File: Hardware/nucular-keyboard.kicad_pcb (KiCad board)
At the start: 2 copper layers, 48 x 25 mm, 34 parts, among them IC1 STM32L052R6Tx, J1 JAE_AA01B-S040VA1, J2 JAE_KX14-40K2D, J3 CONN_01X16, J4 CONN_01X03, Q1 IRLML6402, U1 MCP1700T-3302E/MB

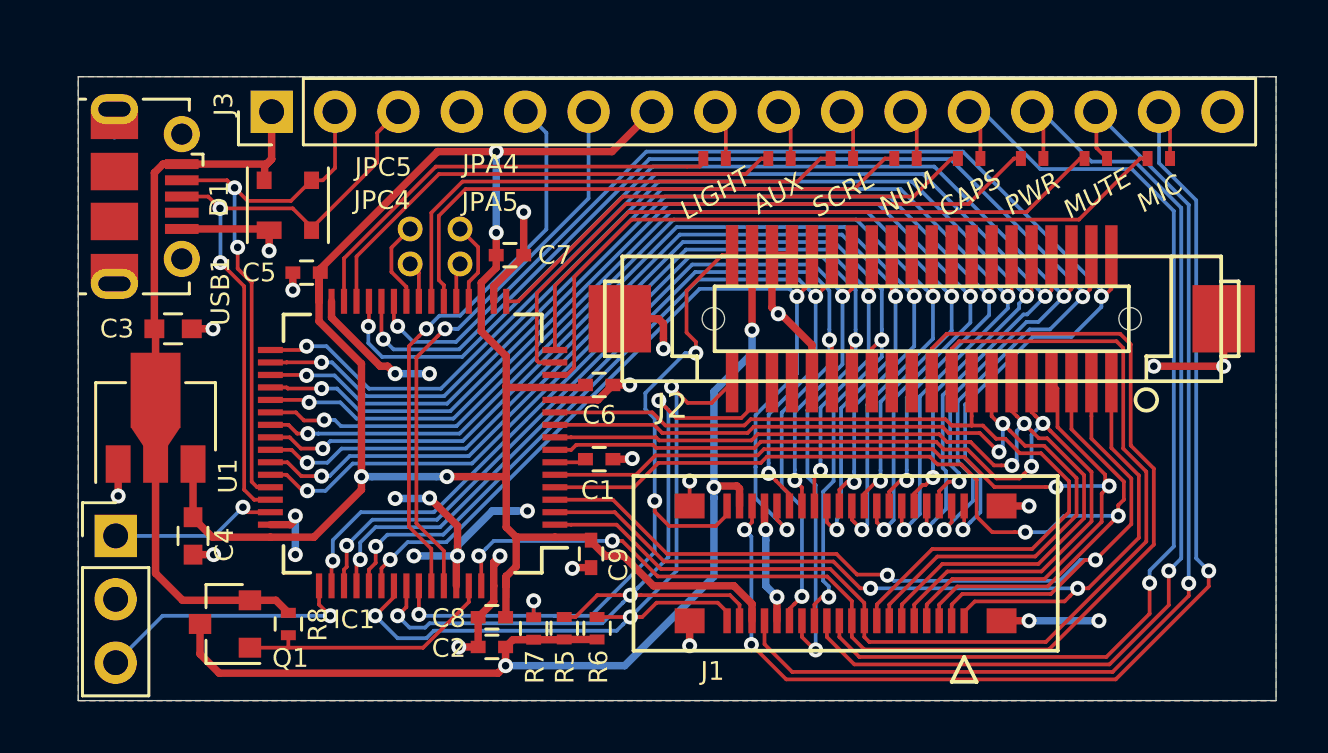
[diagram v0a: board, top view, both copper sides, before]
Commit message: Updated all footprints
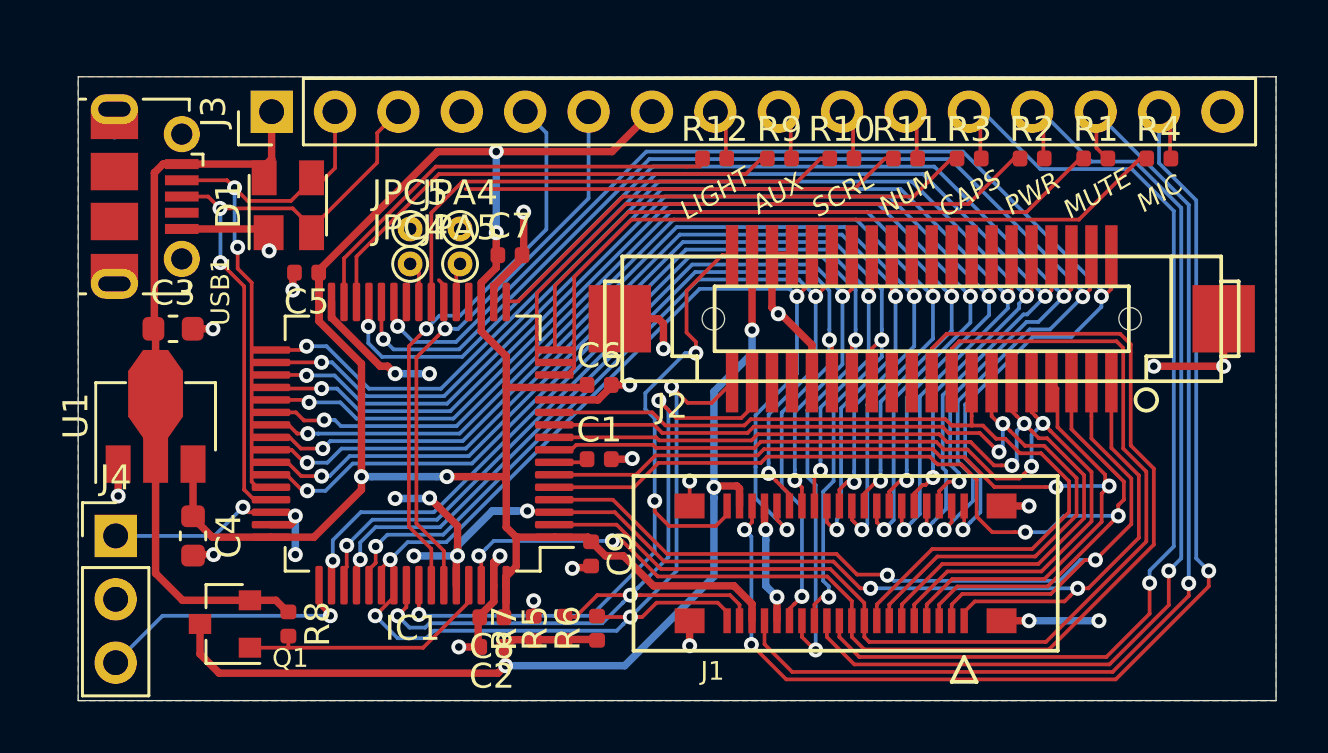
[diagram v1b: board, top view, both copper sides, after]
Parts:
- C1, C2, C5, C6, C7, C8, C9: footprint Capacitors_SMD:C_0402 -> Capacitor_SMD:C_0402_1005Metric
- C3, C4: footprint Capacitors_SMD:C_0603 -> Capacitor_SMD:C_0603_1608Metric
- D1: footprint 000-Modules:SOT143B -> Package_TO_SOT_SMD:SOT-143
- IC1: footprint Housings_QFP:LQFP-64_10x10mm_Pitch0.5mm -> Package_QFP:LQFP-64_10x10mm_P0.5mm
- J3: footprint Pin_Headers:Pin_Header_Straight_1x16_Pitch2.54mm -> Connector_PinHeader_2.54mm:PinHeader_1x16_P2.54mm_Vertical
- J4: footprint Pin_Headers:Pin_Header_Straight_1x03_Pitch2.54mm -> Connector_PinHeader_2.54mm:PinHeader_1x03_P2.54mm_Vertical
- JPA4, JPA5, JPC4, JPC5: footprint Wire_Pads:SolderWirePad_single_0-8mmDrill -> TestPoint:TestPoint_THTPad_D1.0mm_Drill0.5mm
- Q1: footprint TO_SOT_Packages_SMD:SOT-23 -> Package_TO_SOT_SMD:SOT-23
- R1, R10, R11, R12, R2, R3, R4, R9: footprint Resistors_SMD:R_0402_NoSilk -> Resistor_SMD:R_0402_1005Metric
- R5, R6, R7, R8: footprint Resistors_SMD:R_0402 -> Resistor_SMD:R_0402_1005Metric
- U1: footprint 000-Modules:SOT89-3 -> Package_TO_SOT_SMD:SOT-89-3
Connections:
- J2 pad 21: Net-(J2-Pad21) -> (no net)
- J2 pad 23: Net-(J2-Pad23) -> (no net)
- J2 pad 33: Net-(J2-Pad33) -> (no net)
- J2 pad 35: Net-(J2-Pad35) -> (no net)
- USB1 pad 4: Net-(USB1-Pad4) -> (no net)
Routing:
- net /LED_NUM: track 22.7 -> 18.6 mm
- net Net-(IC1-Pad25): track 3.46 -> 0.00 mm
- net Net-(IC1-Pad20): track 3.36 -> 0.00 mm

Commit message: Fixed some clearances
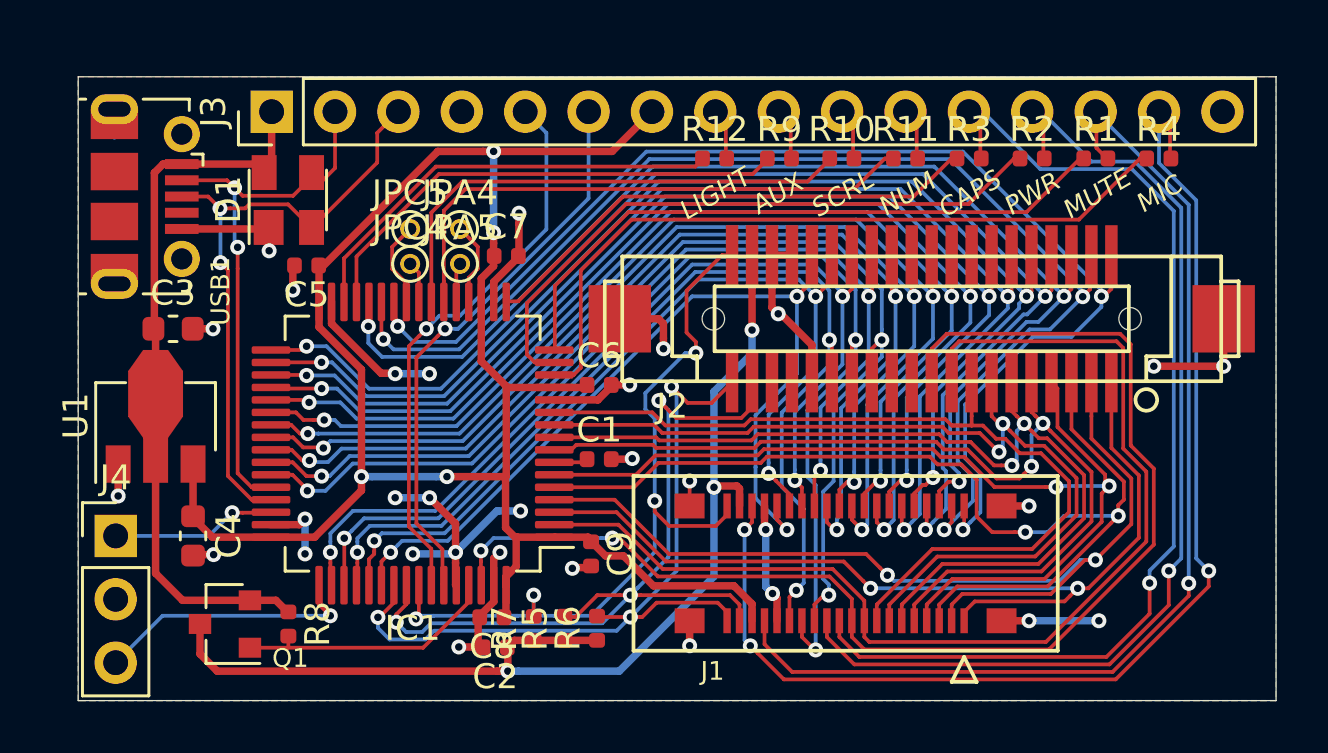
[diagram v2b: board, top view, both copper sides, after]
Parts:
- moved C5 0.29 mm to (69.2, 67.6)
- moved D1 0.21 mm to (68.4, 64.9)
- moved C7 0.15 mm to (77.2, 67.2)
- moved C2 0.13 mm to (76.7, 82.9)
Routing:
- net /LED_NUM: track 18.6 -> 22.6 mm
- net Net-(IC1-Pad25): track 0.00 -> 3.46 mm
- net Net-(IC1-Pad20): track 0.00 -> 3.37 mm
- net GND: track 69.6 -> 67.9 mm
- net VCC: track 77.1 -> 75.9 mm
- net /TP4_RESET: track 31.6 -> 32.4 mm

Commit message: Finished routing
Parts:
- C1, C2, C5, C6, C7, C8, C9: footprint Capacitor_SMD:C_0402_1005Metric -> Capacitor_SMD:C_0603_1608Metric
- R1, R10, R11, R12, R2, R3, R4, R5, R6, R7, R8, R9: footprint Resistor_SMD:R_0402_1005Metric -> Resistor_SMD:R_0603_1608Metric
- moved C2 5.97 mm to (70.7, 82.9), turned to 90 degrees
- moved R12 2.65 mm to (82.9, 63.0)
- moved R9 2.20 mm to (85.9, 63.0)
- moved R10 1.72 mm to (88.9, 63.0)
- moved R11 1.23 mm to (91.9, 63.0)
- moved C8 1.13 mm to (75.6, 82.2)
- moved C6 1.00 mm to (81.7, 73.0)
- moved R7 0.91 mm to (77.9, 82.9)
- moved R6 0.84 mm to (80.9, 82.9)
- moved R5 0.84 mm to (79.4, 82.9)
- moved R4 0.82 mm to (104.1, 63.0)
- moved C1 0.79 mm to (81.7, 75.3)
- moved R3 0.75 mm to (95.0, 63.0)
- moved J3 0.69 mm to (67.8, 60.7)
- moved D1 0.63 mm to (68.5, 64.3)
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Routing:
- net GND: track 67.9 -> 62.5 mm, vias 31 -> 26
- net /+5V_TP: track 43.6 -> 40.5 mm
- net /LED_LIGHT: track 17.8 -> 15.2 mm
- net /LED_AUX: track 19.9 -> 17.8 mm
- net VCC: track 75.9 -> 77.7 mm
- net /LED_LIGHT_R: track 2.02 -> 3.80 mm
- net /LED_MIC_R: track 48.3 -> 49.8 mm
- net /USB_DM: track 22.2 -> 23.7 mm
- net /LED_SCROLL: track 20.5 -> 19.0 mm
- net /LED_MUTE_R: track 42.7 -> 44.1 mm
- net /TP4_PWR: track 10.7 -> 11.9 mm
- net Net-(IC1-Pad20): track 3.37 -> 4.34 mm
- net /LED_NUM: track 22.6 -> 21.7 mm
- net /LED_MIC: track 29.7 -> 30.5 mm
- net /LED_AUX_R: track 2.07 -> 2.88 mm
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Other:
- board size 48 x 25 mm -> 48 x 26 mm

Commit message: Moved references
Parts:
- moved J4 0.19 mm to (61.6, 78.2)

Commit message: Remove silkscreen for testpads
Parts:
- moved JPA5 0.19 mm to (75.3, 67.3)
- moved JPC4 0.19 mm to (73.3, 67.3)
- moved JPA4 0.19 mm to (75.3, 65.9)
- moved JPC5 0.19 mm to (73.3, 65.9)
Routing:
- net Net-(IC1-Pad25): track 3.46 -> 4.34 mm
- net Net-(IC1-Pad20): track 4.34 -> 3.51 mm
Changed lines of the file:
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@@
     (thickness 0.8)
     (drawings 14)
-    (tracks 1191)
+    (tracks 1192)
     (zones 0)
     (modules 34)
@@
     (visible_elements 7FFFFFFF)
     (pcbplotparams
-      (layerselection 0x00030_ffffffff)
+      (layerselection 0x010fc_ffffffff)
       (usegerberextensions false)
       (usegerberattributes false)
@@
       (outputformat 1)
       (mirror false)
-      (drillshape 1)
+      (drillshape 0)
       (scaleselection 1)
-      (outputdirectory ""))
+      (outputdirectory "gerber/"))
   )
   (net 0 "")
@@
     (uvia_drill 0.1)
   )
+  (module TestPoint:TestPoint_THTPad_D1.0mm_Drill0.5mm (layer F.Cu)
+    (at 75.3 67.31)
+    (descr "THT pad as test Point, diameter 1.0mm, hole diameter 0.5mm")
+    (tags "test point THT pad")
+    (attr virtual)
+    (fp_text reference JPA5 (at 1.0905 -2.857) (layer F.SilkS)
+      (effects (font (size 0.75 0.75) (thickness 0.15)))
+    )
+    (fp_text value TEST_1P (at 0 1.55) (layer F.Fab)
+      (effects (font (size 1 1) (thickness 0.15)))
+    )
+    (fp_text user %R (at 0 -1.45) (layer F.Fab)
+      (effects (font (size 0.75 0.75) (thickness 0.15)))
+    )
+    (pad 1 thru_hole circle (at 0 0) (size 0.8 0.8) (drill 0.5) (layers *.Cu *.Mask)
+      (net 3 "Net-(IC1-Pad21)"))
+  )
+  (module TestPoint:TestPoint_THTPad_D1.0mm_Drill0.5mm (layer F.Cu)
+    (at 75.3 65.913)
+    (descr "THT pad as test Point, diameter 1.0mm, hole diameter 0.5mm")
+    (tags "test point THT pad")
+    (attr virtual)
+    (fp_text reference JPA4 (at 1.0905 -2.854) (layer F.SilkS)
+      (effects (font (size 0.75 0.75) (thickness 0.15)))
+    )
+    (fp_text value TEST_1P (at 0 1.55) (layer F.Fab)
+      (effects (font (size 1 1) (thickness 0.15)))
+    )
+    (fp_text user %R (at 0 -1.45) (layer F.Fab)
+      (effects (font (size 0.75 0.75) (thickness 0.15)))
+    )
+    (pad 1 thru_hole circle (at 0 0) (size 0.8 0.8) (drill 0.5) (layers *.Cu *.Mask)
+      (net 4 "Net-(IC1-Pad20)"))
+  )
+  (module TestPoint:TestPoint_THTPad_D1.0mm_Drill0.5mm (layer F.Cu)
+    (at 73.3 67.31)
+    (descr "THT pad as test Point, diameter 1.0mm, hole diameter 0.5mm")
+    (tags "test point THT pad")
+    (attr virtual)
+    (fp_text reference JPC4 (at -0.9735 -2.857) (layer F.SilkS)
+      (effects (font (size 0.75 0.75) (thickness 0.15)))
+    )
+    (fp_text value TEST_1P (at 0 1.55) (layer F.Fab)
+      (effects (font (size 1 1) (thickness 0.15)))
+    )
+    (fp_text user %R (at 0 -1.45) (layer F.Fab)
+      (effects (font (size 0.75 0.75) (thickness 0.15)))
+    )
+    (pad 1 thru_hole circle (at 0 0) (size 0.8 0.8) (drill 0.5) (layers *.Cu *.Mask)
+      (net 6 "Net-(IC1-Pad24)"))
+  )
+  (module TestPoint:TestPoint_THTPad_D1.0mm_Drill0.5mm (layer F.Cu)
+    (at 73.3 65.913)
+    (descr "THT pad as test Point, diameter 1.0mm, hole diameter 0.5mm")
+    (tags "test point THT pad")
+    (attr virtual)
+    (fp_text reference JPC5 (at -0.9735 -2.854) (layer F.SilkS)
+      (effects (font (size 0.75 0.75) (thickness 0.15)))
+    )
+    (fp_text value TEST_1P (at 0 1.55) (layer F.Fab)
+      (effects (font (size 1 1) (thickness 0.15)))
+    )
+    (fp_text user %R (at 0 -1.45) (layer F.Fab)
+      (effects (font (size 0.75 0.75) (thickness 0.15)))
+    )
+    (pad 1 thru_hole circle (at 0 0) (size 0.8 0.8) (drill 0.5) (layers *.Cu *.Mask)
+      (net 5 "Net-(IC1-Pad25)"))
+  )
   (module Connector_PinHeader_2.54mm:PinHeader_1x16_P2.54mm_Vertical locked (layer F.Cu)
     (at 67.75 60.706 90)
@@
       (rotate (xyz 0 0 0))
     )
-  )
-  (module TestPoint:TestPoint_THTPad_D1.0mm_Drill0.5mm (layer F.Cu)
-    (at 75.3 67.5)
-    (descr "THT pad as test Point, diameter 1.0mm, hole diameter 0.5mm")
-    (tags "test point THT pad")
-    (attr virtual)
-    (fp_text reference JPA5 (at 1.0905 -2.857) (layer F.SilkS)
-      (effects (font (size 0.75 0.75) (thickness 0.15)))
-    )
-    (fp_text value TEST_1P (at 0 1.55) (layer F.Fab)
-      (effects (font (size 1 1) (thickness 0.15)))
-    )
-    (fp_circle (center 0 0) (end 0 0.7) (layer F.SilkS) (width 0.15))
-    (fp_text user %R (at 0 -1.45) (layer F.Fab)
-      (effects (font (size 0.75 0.75) (thickness 0.15)))
-    )
-    (pad 1 thru_hole circle (at 0 0) (size 0.8 0.8) (drill 0.5) (layers *.Cu *.Mask)
-      (net 3 "Net-(IC1-Pad21)"))
-  )
-  (module TestPoint:TestPoint_THTPad_D1.0mm_Drill0.5mm (layer F.Cu)
-    (at 75.3 66.1)
-    (descr "THT pad as test Point, diameter 1.0mm, hole diameter 0.5mm")
-    (tags "test point THT pad")
-    (attr virtual)
-    (fp_text reference JPA4 (at 1.0905 -2.854) (layer F.SilkS)
-      (effects (font (size 0.75 0.75) (thickness 0.15)))
-    )
-    (fp_text value TEST_1P (at 0 1.55) (layer F.Fab)
-      (effects (font (size 1 1) (thickness 0.15)))
-    )
-    (fp_text user %R (at 0 -1.45) (layer F.Fab)
-      (effects (font (size 0.75 0.75) (thickness 0.15)))
-    )
-    (fp_circle (center 0 0) (end 0 0.7) (layer F.SilkS) (width 0.15))
-    (pad 1 thru_hole circle (at 0 0) (size 0.8 0.8) (drill 0.5) (layers *.Cu *.Mask)
-      (net 4 "Net-(IC1-Pad20)"))
-  )
-  (module TestPoint:TestPoint_THTPad_D1.0mm_Drill0.5mm (layer F.Cu)
-    (at 73.3 66.1)
-    (descr "THT pad as test Point, diameter 1.0mm, hole diameter 0.5mm")
-    (tags "test point THT pad")
-    (attr virtual)
-    (fp_text reference JPC5 (at -0.9735 -2.854) (layer F.SilkS)
-      (effects (font (size 0.75 0.75) (thickness 0.15)))
-    )
-    (fp_text value TEST_1P (at 0 1.55) (layer F.Fab)
-      (effects (font (size 1 1) (thickness 0.15)))
-    )
-    (fp_circle (center 0 0) (end 0 0.7) (layer F.SilkS) (width 0.15))
-    (fp_text user %R (at 0 -1.45) (layer F.Fab)
-      (effects (font (size 0.75 0.75) (thickness 0.15)))
-    )
-    (pad 1 thru_hole circle (at 0 0) (size 0.8 0.8) (drill 0.5) (layers *.Cu *.Mask)
-      (net 5 "Net-(IC1-Pad25)"))
-  )
-  (module TestPoint:TestPoint_THTPad_D1.0mm_Drill0.5mm (layer F.Cu)
-    (at 73.3 67.5)
-    (descr "THT pad as test Point, diameter 1.0mm, hole diameter 0.5mm")
-    (tags "test point THT pad")
-    (attr virtual)
-    (fp_text reference JPC4 (at -0.9735 -2.857) (layer F.SilkS)
-      (effects (font (size 0.75 0.75) (thickness 0.15)))
-    )
-    (fp_text value TEST_1P (at 0 1.55) (layer F.Fab)
-      (effects (font (size 1 1) (thickness 0.15)))
-    )
-    (fp_text user %R (at 0 -1.45) (layer F.Fab)
-      (effects (font (size 0.75 0.75) (thickness 0.15)))
-    )
-    (fp_circle (center 0 0) (end 0 0.7) (layer F.SilkS) (width 0.15))
-    (pad 1 thru_hole circle (at 0 0) (size 0.8 0.8) (drill 0.5) (layers *.Cu *.Mask)
-      (net 6 "Net-(IC1-Pad24)"))
   )
   (module Resistor_SMD:R_0603_1608Metric (layer F.Cu)
@@
   (segment (start 78.321 66.802) (end 78.321 66.129) (width 0.3) (layer F.Cu) (net 2))
   (segment (start 61.45 61.743) (end 61.45 63.643) (width 0.3) (layer F.Cu) (net 2))
-  (segment (start 75.15 69) (end 75.15 67.65) (width 0.15) (layer F.Cu) (net 3) (status 30))
-  (segment (start 75.15 67.65) (end 75.3 67.5) (width 0.15) (layer F.Cu) (net 3) (status 30))
-  (segment (start 75.65 69.025) (end 75.65 68.052898) (width 0.15) (layer F.Cu) (net 4) (status 10))
+  (segment (start 75.15 67.46) (end 75.3 67.31) (width 0.15) (layer F.Cu) (net 3))
+  (segment (start 75.15 69.025) (end 75.15 67.46) (width 0.15) (layer F.Cu) (net 3))
   (segment (start 75.65 68.25) (end 75.65 69.025) (width 0.15) (layer F.Cu) (net 4))
-  (segment (start 76.0095 67.693399) (end 75.65 68.052899) (width 0.15) (layer F.Cu) (net 4))
-  (segment (start 76.0095 66.8095) (end 76.0095 67.693399) (width 0.15) (layer F.Cu) (net 4))
+  (segment (start 75.311 65.913) (end 75.946 66.548) (width 0.15) (layer F.Cu) (net 4))
+  (segment (start 75.3 65.913) (end 75.311 65.913) (width 0.15) (layer F.Cu) (net 4))
+  (segment (start 75.946 66.548) (end 75.946 67.756899) (width 0.15) (layer F.Cu) (net 4))
+  (segment (start 75.946 67.756899) (end 75.65 68.052899) (width 0.15) (layer F.Cu) (net 4))
   (segment (start 75.65 68.052899) (end 75.65 68.25) (width 0.15) (layer F.Cu) (net 4))
-  (segment (start 75.3 66.1) (end 76.0095 66.8095) (width 0.15) (layer F.Cu) (net 4))
-  (segment (start 72.800001 66.599999) (end 73.3 66.1) (width 0.15) (layer F.Cu) (net 5) (status 20))
-  (segment (start 72.5805 66.8195) (end 72.800001 66.599999) (width 0.15) (layer F.Cu) (net 5))
-  (segment (start 72.5805 67.705502) (end 72.5805 66.8195) (width 0.15) (layer F.Cu) (net 5))
   (segment (start 73.15 69.025) (end 73.15 68.275002) (width 0.15) (layer F.Cu) (net 5) (status 30))
-  (segment (start 73.15 68.275002) (end 72.5805 67.705502) (width 0.15) (layer F.Cu) (net 5) (status 10))
-  (segment (start 73.65 69) (end 73.65 67.85) (width 0.15) (layer F.Cu) (net 6) (status 10))
-  (segment (start 73.65 67.85) (end 73.3 67.5) (width 0.15) (layer F.Cu) (net 6) (status 20))
+  (segment (start 72.644 66.569) (end 73.3 65.913) (width 0.15) (layer F.Cu) (net 5))
+  (segment (start 72.644 67.579002) (end 72.644 66.569) (width 0.15) (layer F.Cu) (net 5))
+  (segment (start 73.15 69.025) (end 73.15 68.085002) (width 0.15) (layer F.Cu) (net 5))
+  (segment (start 73.15 68.085002) (end 72.644 67.579002) (width 0.15) (layer F.Cu) (net 5))
+  (segment (start 73.699999 68.975001) (end 73.65 69.025) (width 0.15) (layer F.Cu) (net 6))
+  (segment (start 73.699999 67.709999) (end 73.699999 68.975001) (width 0.15) (layer F.Cu) (net 6))
+  (segment (start 73.3 67.31) (end 73.699999 67.709999) (width 0.15) (layer F.Cu) (net 6))
   (segment (start 66.88 82.88) (end 68.4 82.88) (width 0.15) (layer F.Cu) (net 7) (status 30))
   (segment (start 68.42 82.38) (end 68.42 82.86) (width 0.15) (layer F.Cu) (net 7) (status 30))
